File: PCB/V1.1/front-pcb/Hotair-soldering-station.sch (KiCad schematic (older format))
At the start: 60 parts, among them J2 main-board-conn, J3 hot_on, J4 solder_on, Q1 BC817, Q10 BC807, Q11 BC807, Q12 BC807, Q13 BC807, Q14 BC807, Q2 BC817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

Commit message: Main board routing, remove old 7seg from front panel schematic
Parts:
- removed Q1, Q2, Q3, Q4, Q5, Q6, Q7, Q8: BC817, Package_TO_SOT_SMD:SOT-23, symbol Transistor_BJT:BC817
- removed Q10, Q11, Q12, Q13, Q14, Q9: BC807, Package_TO_SOT_SMD:SOT-23, symbol Transistor_BJT:BC807
- removed R1, R17, R18, R19, R2, R20, R21, R22, R3, R4, R5, R7, R8: 10k, Capacitors:0805, symbol Device:R
- removed R10, R11, R12, R13, R14, R15, R16, R9: 120R, Capacitors:0805, symbol Device:R
- removed R6: 5k6, Capacitors:0805, symbol Device:R
- removed U3: My-Footprints:3-digit-7-segment-display, My-Footprints:3-digit-7-segment-display, symbol Hotair-soldering-station-rescue:3-dig-7-seg-display-common-anode-My-Lib
- removed U4: 3-dig-7-seg-display-common-anode, My-Footprints:3-digit-7-segment-display, symbol Hotair-soldering-station-rescue:3-dig-7-seg-display-common-anode-My-Lib
- added U?: RC1602A, Display:RC1602A, symbol Display_Character:RC1602A
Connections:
- net labels added: +5V, LCD_DB4, LCD_DB5, LCD_DB6, LCD_DB7, LCD_E, LCD_RS
- net labels removed: HOTAIR_DIG1, HOTAIR_DIG2, HOTAIR_DIG3, IRON_DIG1, IRON_DIG2, IRON_DIG3, SEG_A, SEG_B, SEG_C, SEG_D, SEG_DP, SEG_E, SEG_F, SEG_G
- wire segments 263 -> 125
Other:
- note removed: "1,75V @ 10mA\n1,78V @ 15mA"
- note removed: "8x120R"

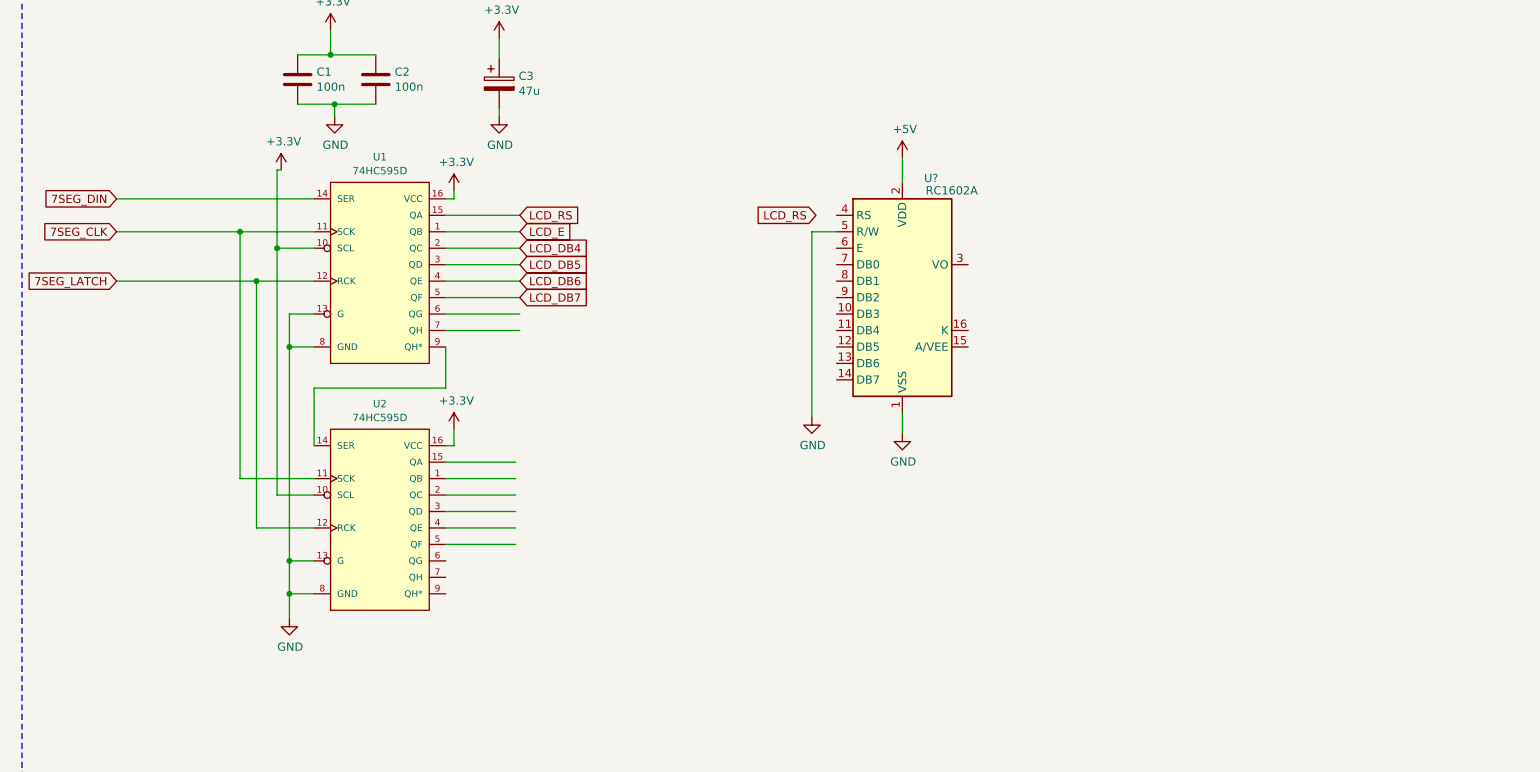
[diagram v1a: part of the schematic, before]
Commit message: uC change to STM32F103
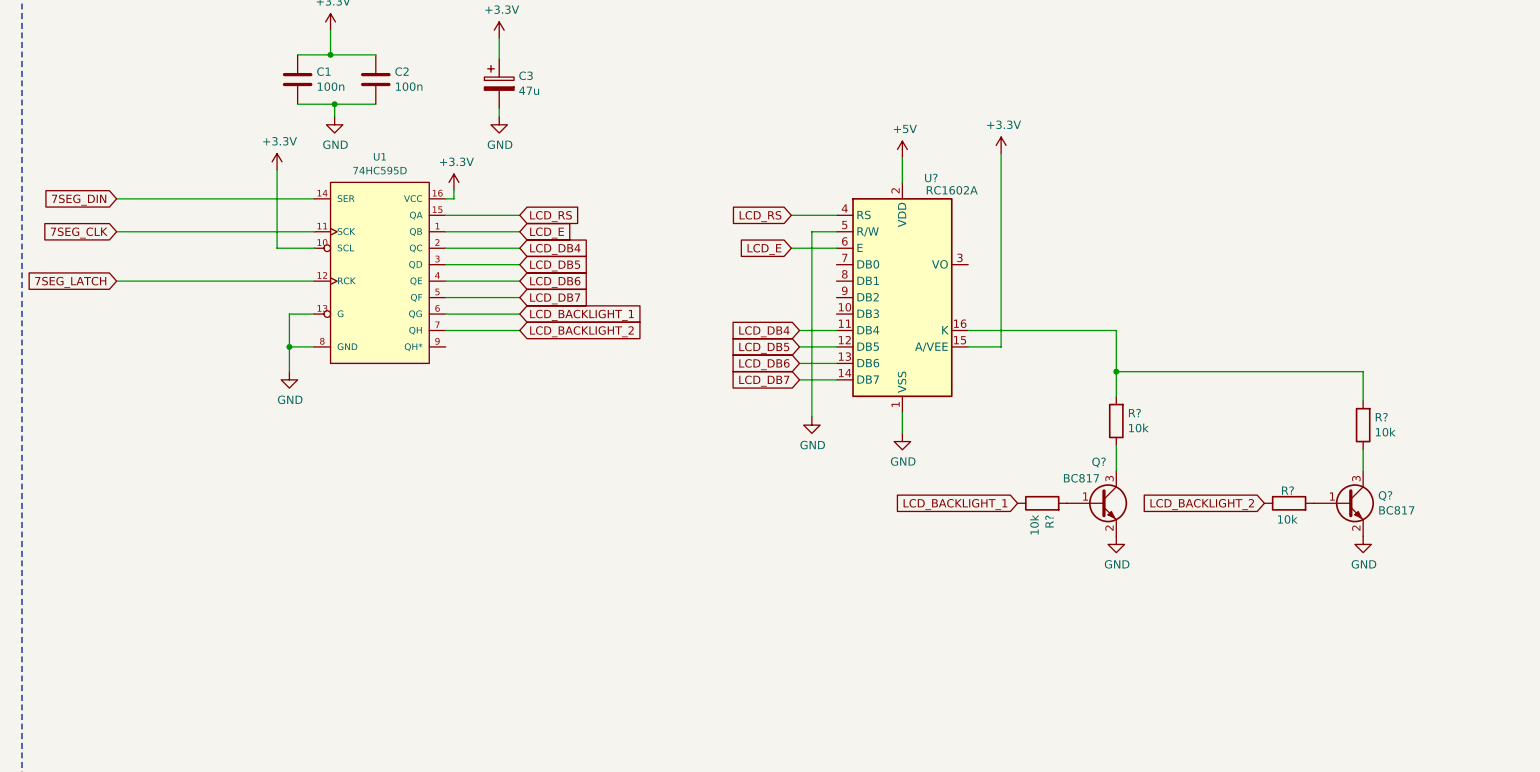
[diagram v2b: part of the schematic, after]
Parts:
- removed U2: 74HC595D, Silicon-Standard:SO16, symbol SparkFun-IC-Logic:74HC595D
- added Q? (x2): BC817, Package_TO_SOT_SMD:SOT-23, symbol Transistor_BJT:BC817
- added R? (x4): 10k, Capacitors:0805, symbol Device:R
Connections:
- net labels added: LCD_BACKLIGHT_1, LCD_BACKLIGHT_2
- wire segments 125 -> 116
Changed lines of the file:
@@
 	3825 6375 3375 6375
-Wire Wire Line
-	3425 7775 3425 7675
-Wire Wire Line
-	3375 7775 3425 7775
-$Comp
-L power:+3.3V #PWR0111
-U 1 1 5F7CBAA3
-P 3425 7675
-F 0 "#PWR0111" H 3425 7525 50  0001 C CNN
-F 1 "+3.3V" H 3440 7848 50  0000 C CNN
-F 2 "" H 3425 7675 50  0001 C CNN
-F 3 "" H 3425 7675 50  0001 C CNN
-	1    3425 7675
-	1    0    0    -1
-$EndComp
 Wire Wire Line
 	3425 6275 3425 6225
@@
 7SEG_DIN
 Wire Wire Line
-	3375 7425 3375 7175
-Wire Wire Line
-	2575 7425 3375 7425
-Wire Wire Line
-	2575 7775 2575 7425
-Wire Wire Line
 	1375 6275 2575 6275
-Connection ~ 2225 6775
-Wire Wire Line
-	2225 6775 1375 6775
-Connection ~ 2125 6475
-Wire Wire Line
-	2125 6475 1375 6475
-Wire Wire Line
-	2225 8275 2575 8275
-Wire Wire Line
-	2225 6775 2225 8275
-Wire Wire Line
-	2575 6775 2225 6775
-Connection ~ 2425 7175
 Wire Wire Line
 	2425 6975 2425 7175
@@
 Wire Wire Line
 	2575 7175 2425 7175
-Wire Wire Line
-	2425 8475 2425 8675
-Connection ~ 2425 8475
-Wire Wire Line
-	2575 8475 2425 8475
-Connection ~ 2425 8675
-Wire Wire Line
-	2425 8675 2425 8825
-Wire Wire Line
-	2575 8675 2425 8675
-$Comp
-L power:GND #PWR0113
-U 1 1 5F7A79C4
-P 2425 8825
-F 0 "#PWR0113" H 2425 8575 50  0001 C CNN
-F 1 "GND" H 2430 8652 50  0000 C CNN
-F 2 "" H 2425 8825 50  0001 C CNN
-F 3 "" H 2425 8825 50  0001 C CNN
-	1    2425 8825
-	1    0    0    -1
-$EndComp
-Wire Wire Line
-	2125 7975 2575 7975
-Wire Wire Line
-	2125 6475 2125 7975
-Wire Wire Line
-	2575 6475 2125 6475
-$Comp
-L SparkFun-IC-Logic:74HC595D U2
-U 1 1 5F7A37BF
-P 2975 8225
-F 0 "U2" H 2975 8929 45  0000 C CNN
-F 1 "74HC595D" H 2975 8845 45  0000 C CNN
-F 2 "Silicon-Standard:SO16" H 2975 8925 20  0001 C CNN
-F 3 "" H 2975 8225 50  0001 C CNN
-F 4 "" H 2875 8275 60  0001 C CNN "Pole4"
-	1    2975 8225
-	1    0    0    -1
-$EndComp
 $Comp
 L SparkFun-IC-Logic:74HC595D U1
@@
 	1    0    0    -1
 $EndComp
-Wire Wire Line
-	3800 7875 3375 7875
-Wire Wire Line
-	3375 7975 3800 7975
-Wire Wire Line
-	3375 8175 3800 8175
-Wire Wire Line
-	3800 8275 3375 8275
-Wire Wire Line
-	3800 8375 3375 8375
 Wire Notes Line
 	11300 10725 11300 4725
@@
 SMD Rework, Soldering station - Front PCB
 Wire Wire Line
-	3375 8075 3800 8075
-Wire Wire Line
 	3825 7075 3375 7075
 $Comp
@@
 	3700 5725 3700 5775
 Wire Wire Line
-	2425 7175 2425 8475
-Wire Wire Line
-	2575 8075 2350 8075
-Wire Wire Line
-	2350 8075 2350 6575
-Wire Wire Line
 	2350 6575 2575 6575
 $Comp
 L power:+3.3V #PWR?
 U 1 1 5FF4B733
-P 2375 6100
-F 0 "#PWR?" H 2375 5950 50  0001 C CNN
-F 1 "+3.3V" H 2390 6273 50  0000 C CNN
-F 2 "" H 2375 6100 50  0001 C CNN
-F 3 "" H 2375 6100 50  0001 C CNN
-	1    2375 6100
+P 2350 6100
+F 0 "#PWR?" H 2350 5950 50  0001 C CNN
+F 1 "+3.3V" H 2365 6273 50  0000 C CNN
+F 2 "" H 2350 6100 50  0001 C CNN
+F 3 "" H 2350 6100 50  0001 C CNN
+	1    2350 6100
 	1    0    0    -1
 $EndComp
 Wire Wire Line
 	2350 6575 2350 6100
-Wire Wire Line
-	2350 6100 2375 6100
-Connection ~ 2350 6575
 $Comp
 L Display_Character:RC1602A U?
@@
 Wire Wire Line
 	6150 7575 6150 7700
-Text GLabel 5625 6375 0    50   Input ~ 0
-LCD_RS
 $Comp
 L power:GND #PWR?
@@
 Wire Wire Line
 	5600 6475 5600 7600
+Wire Wire Line
+	1375 6775 2575 6775
+Wire Wire Line
+	1375 6475 2575 6475
+$Comp
+L power:GND #PWR?
+U 1 1 6147FA1B
+P 2425 7325
+F 0 "#PWR?" H 2425 7075 50  0001 C CNN
+F 1 "GND" H 2430 7152 50  0000 C CNN
+F 2 "" H 2425 7325 50  0001 C CNN
+F 3 "" H 2425 7325 50  0001 C CNN
+	1    2425 7325
+	1    0    0    -1
+$EndComp
+Wire Wire Line
+	2425 7325 2425 7175
+Connection ~ 2425 7175
+Text GLabel 5475 6375 0    50   Input ~ 0
+LCD_RS
+Text GLabel 5475 6575 0    50   Input ~ 0
+LCD_E
+Text GLabel 5525 7075 0    50   Input ~ 0
+LCD_DB4
+Text GLabel 5525 7175 0    50   Input ~ 0
+LCD_DB5
+Text GLabel 5525 7275 0    50   Input ~ 0
+LCD_DB6
+Text GLabel 5525 7375 0    50   Input ~ 0
+LCD_DB7
+Wire Wire Line
+	5750 7075 5525 7075
+Wire Wire Line
+	5750 7175 5525 7175
+Wire Wire Line
+	5750 7275 5525 7275
+Wire Wire Line
+	5750 7375 5525 7375
+Wire Wire Line
+	5475 6575 5750 6575
+Wire Wire Line
+	5750 6375 5475 6375
+$Comp
+L Transistor_BJT:BC817 Q?
+U 1 1 6149EAB6
+P 7350 8125
+F 0 "Q?" H 7300 8375 50  0000 L CNN
+F 1 "BC817" H 7125 8275 50  0000 L CNN
+F 2 "Package_TO_SOT_SMD:SOT-23" H 7550 8050 50  0001 L CIN
+F 3 "http://www.fairchildsemi.com/ds/BC/BC817.pdf" H 7350 8125 50  0001 L CNN
+	1    7350 8125
+	1    0    0    -1
+$EndComp
+$Comp
+L Transistor_BJT:BC817 Q?
+U 1 1 614A0612
+P 8850 8125
+F 0 "Q?" H 9041 8171 50  0000 L CNN
+F 1 "BC817" H 9041 8080 50  0000 L CNN
+F 2 "Package_TO_SOT_SMD:SOT-23" H 9050 8050 50  0001 L CIN
+F 3 "http://www.fairchildsemi.com/ds/BC/BC817.pdf" H 8850 8125 50  0001 L CNN
+	1    8850 8125
+	1    0    0    -1
+$EndComp
+$Comp
+L Device:R R?
+U 1 1 614A1E6D
+P 7450 7625
+F 0 "R?" H 7380 7579 50  0000 R CNN
+F 1 "10k" H 7380 7670 50  0000 R CNN
+F 2 "Capacitors:0805" V 7380 7625 50  0001 C CNN
+F 3 "~" H 7450 7625 50  0001 C CNN
+	1    7450 7625
+	-1   0    0    1
+$EndComp
+$Comp
+L Device:R R?
+U 1 1 614A284D
+P 8950 7650
+F 0 "R?" H 8880 7604 50  0000 R CNN
+F 1 "10k" H 8880 7695 50  0000 R CNN
+F 2 "Capacitors:0805" V 8880 7650 50  0001 C CNN
+F 3 "~" H 8950 7650 50  0001 C CNN
+	1    8950 7650
+	-1   0    0    1
+$EndComp
+Wire Wire Line
+	7450 7325 7450 7475
+Wire Wire Line
+	7450 7325 8950 7325
+Wire Wire Line
+	8950 7325 8950 7500
+Wire Wire Line
+	7450 7775 7450 7925
+Wire Wire Line
+	8950 7800 8950 7925
+Wire Wire Line
+	6550 7075 7450 7075
+Wire Wire Line
+	7450 7075 7450 7325
+Connection ~ 7450 7325
+$Comp
+L power:+3.3V #PWR?
+U 1 1 614C1AB1
+P 6750 6000
+F 0 "#PWR?" H 6750 5850 50  0001 C CNN
+F 1 "+3.3V" H 6765 6173 50  0000 C CNN
+F 2 "" H 6750 6000 50  0001 C CNN
+F 3 "" H 6750 6000 50  0001 C CNN
+	1    6750 6000
+	1    0    0    -1
+$EndComp
+Wire Wire Line
+	6550 7175 6750 7175
+Wire Wire Line
+	6750 7175 6750 6000
+Text GLabel 3825 6975 2    50   Input ~ 0
+LCD_BACKLIGHT_1
+Text GLabel 3825 7075 2    50   Input ~ 0
+LCD_BACKLIGHT_2
+Text GLabel 6850 8125 0    50   Input ~ 0
+LCD_BACKLIGHT_1
+Text GLabel 8350 8125 0    50   Input ~ 0
+LCD_BACKLIGHT_2
+$Comp
+L Device:R R?
+U 1 1 614CD4CB
+P 8500 8125
+F 0 "R?" V 8575 8175 50  0000 R CNN
+F 1 "10k" V 8400 8200 50  0000 R CNN
+F 2 "Capacitors:0805" V 8430 8125 50  0001 C CNN
+F 3 "~" H 8500 8125 50  0001 C CNN
+	1    8500 8125
+	0    -1   -1   0
+$EndComp
+$Comp
+L Device:R R?
+U 1 1 614CDEFA
+P 7000 8125
+F 0 "R?" H 6930 8079 50  0000 R CNN
+F 1 "10k" H 6930 8170 50  0000 R CNN
+F 2 "Capacitors:0805" V 6930 8125 50  0001 C CNN
+F 3 "~" H 7000 8125 50  0001 C CNN
+	1    7000 8125
+	0    -1   -1   0
+$EndComp
+$Comp
+L power:GND #PWR?
+U 1 1 614CE767
+P 7450 8325
+F 0 "#PWR?" H 7450 8075 50  0001 C CNN
+F 1 "GND" H 7455 8152 50  0000 C CNN
+F 2 "" H 7450 8325 50  0001 C CNN
+F 3 "" H 7450 8325 50  0001 C CNN
+	1    7450 8325
+	1    0    0    -1
+$EndComp
+$Comp
+L power:GND #PWR?
+U 1 1 614CED74
+P 8950 8325
+F 0 "#PWR?" H 8950 8075 50  0001 C CNN
+F 1 "GND" H 8955 8152 50  0000 C CNN
+F 2 "" H 8950 8325 50  0001 C CNN
+F 3 "" H 8950 8325 50  0001 C CNN
+	1    8950 8325
+	1    0    0    -1
+$EndComp
 $EndSCHEMATC
